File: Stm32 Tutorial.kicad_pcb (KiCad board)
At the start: 2 copper layers, 44.2 x 32 mm, 32 parts, among them J1 Conn_01x04_Male, J2 Conn_01x04_Male, J3 Conn_01x04_Male, J4 USB_B_Micro, SW1 SW_SPDT, U1 AMS1117-3.3, U2 STM32F103C8T6, Y1 16Mhz

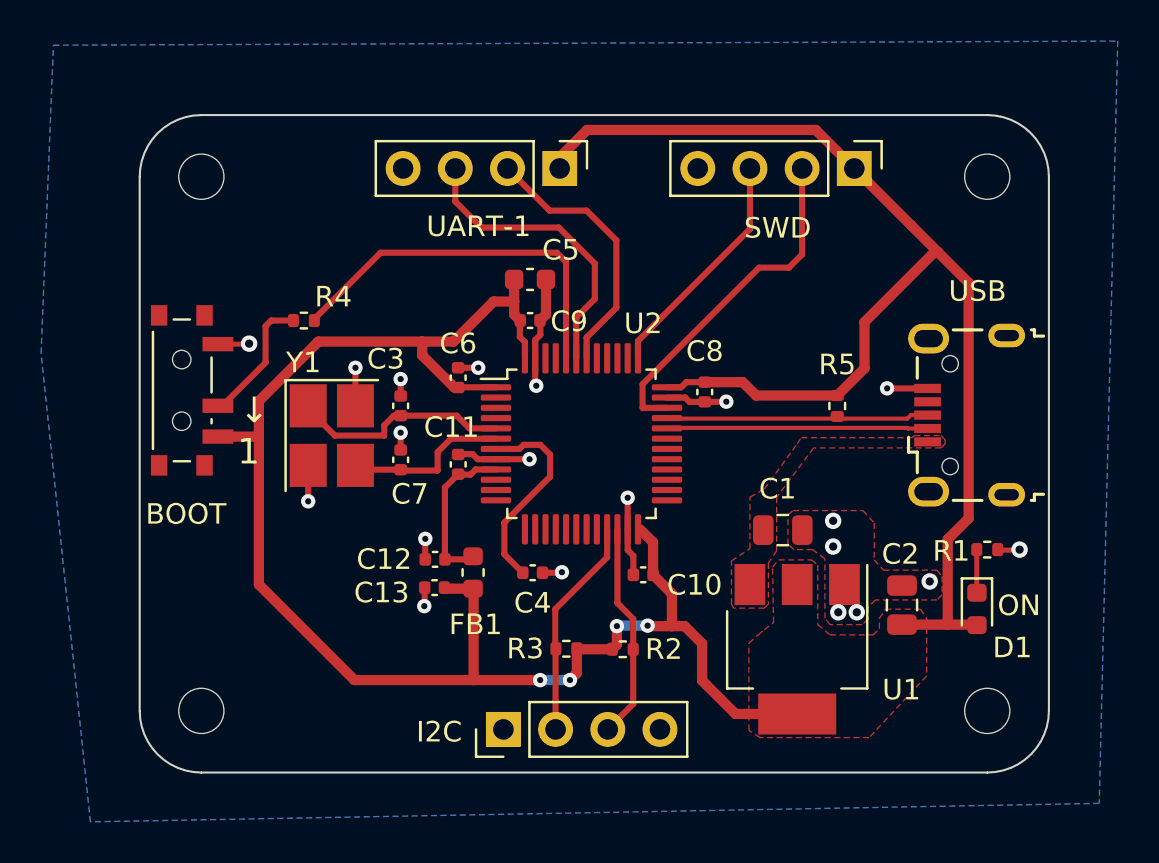
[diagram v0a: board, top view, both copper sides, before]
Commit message: Fixed Missing Track to 3.3V header Pin
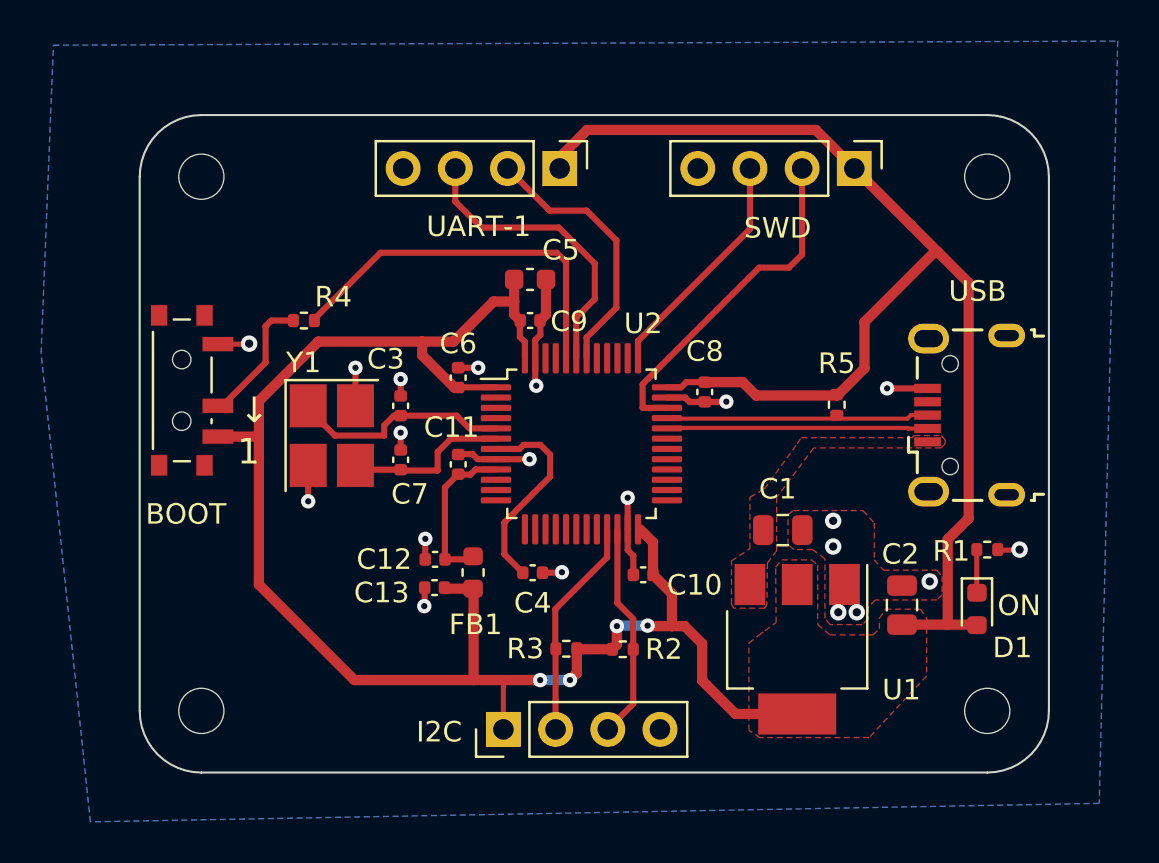
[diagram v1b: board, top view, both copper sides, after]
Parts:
- moved R5 0.06 mm to (167.4, 87.1)
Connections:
- J4 pad 6: unconnected-(J4-Pad6) -> GND
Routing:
- net +3.3V: track 141.5 -> 143.9 mm
- net GND: track 29.5 -> 30.2 mm
